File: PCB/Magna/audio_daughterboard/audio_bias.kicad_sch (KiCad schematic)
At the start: 8 parts, among them U1101 NE5532

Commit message: Some updates to PCB
Honestly I cannot remember whats changed
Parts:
- renumbered C1101 to C801, C1102 to C802, R1101 to R801, R1102 to R802, TP1101 to TP801, TP1102 to TP802, TP1103 to TP803, U1101 to U801

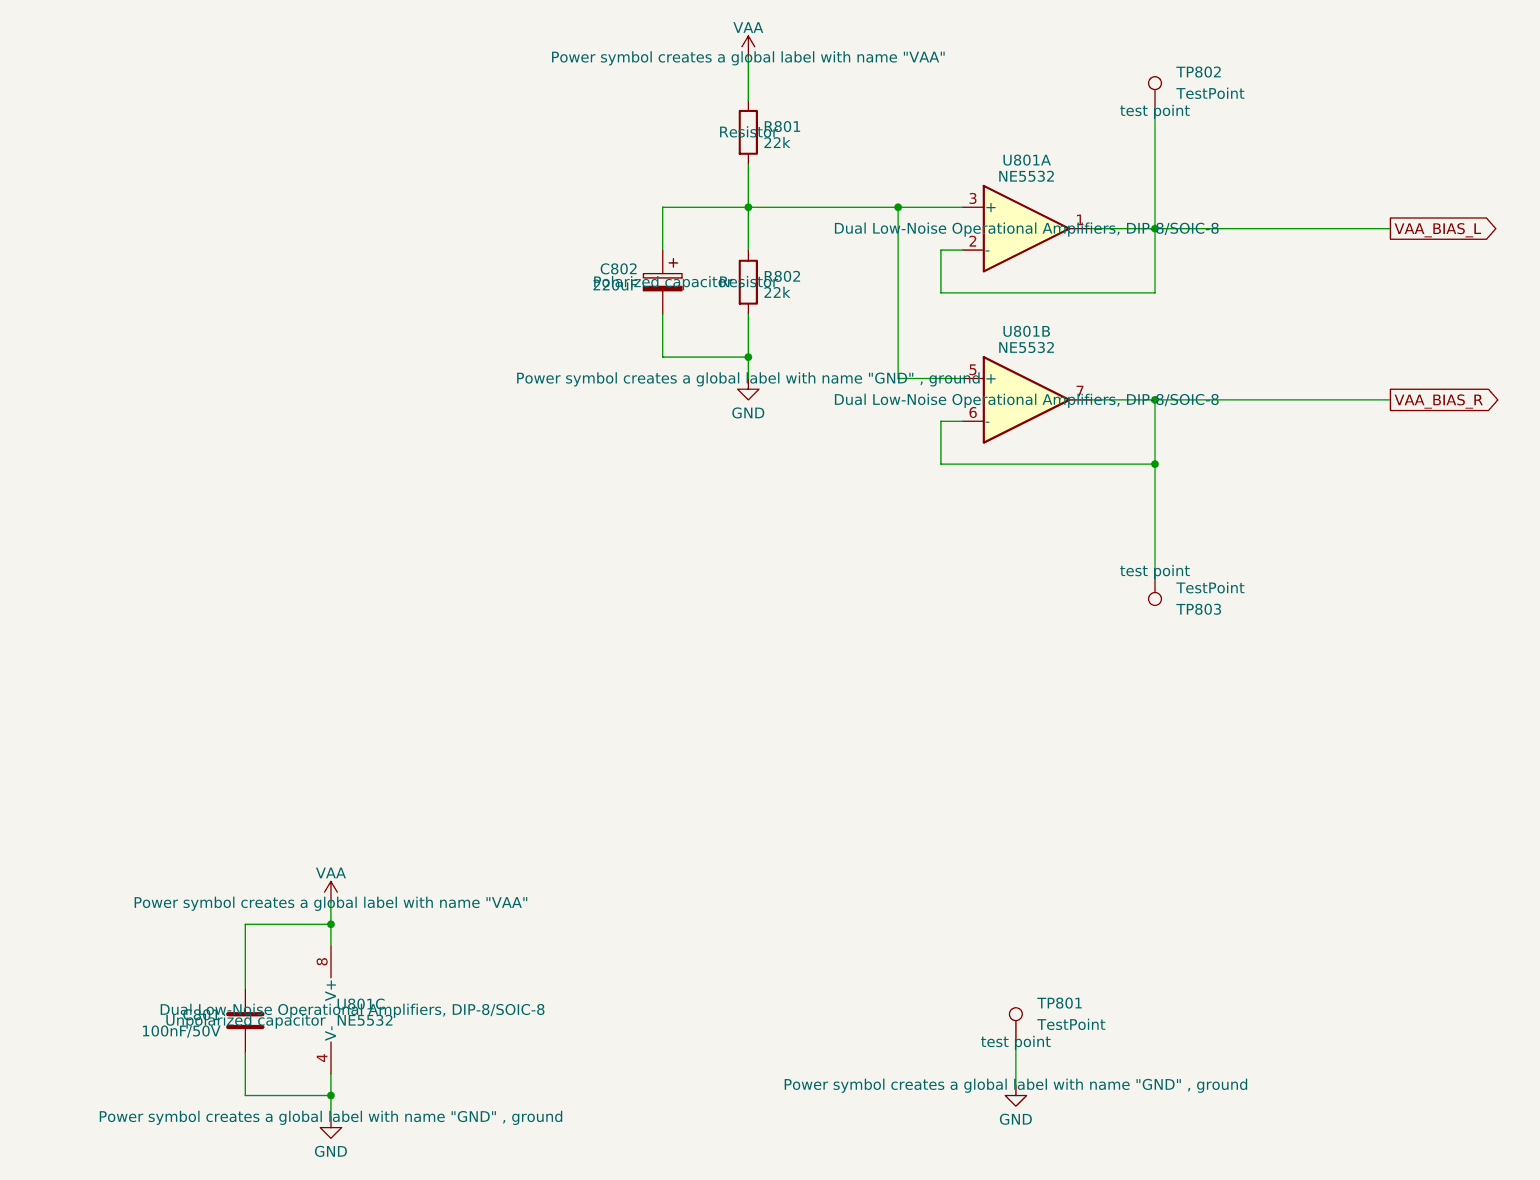
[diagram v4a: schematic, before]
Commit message: Update schematics to Kicad 9
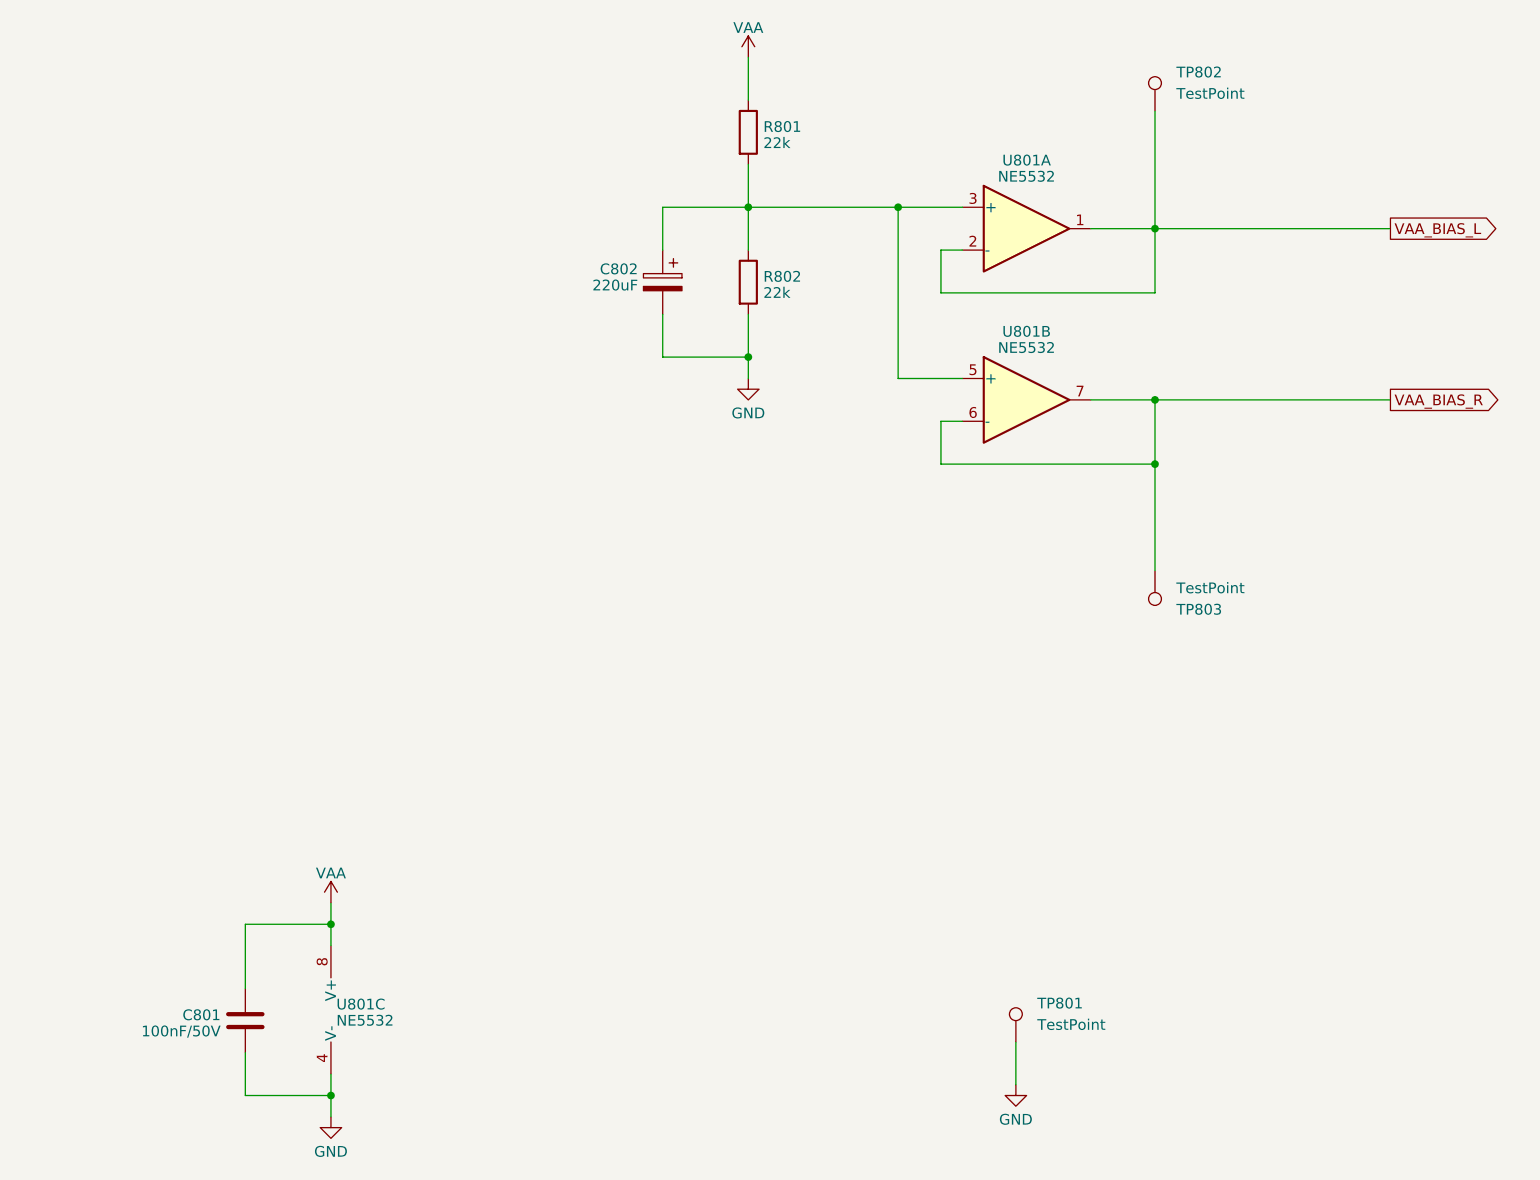
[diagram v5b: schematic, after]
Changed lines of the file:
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@@
 					(size 1.27 1.27)
 				)
+				(hide yes)
 			)
 		)
@@
 					(size 1.27 1.27)
 				)
+				(hide yes)
 			)
 		)
@@
 					(size 1.27 1.27)
 				)
+				(hide yes)
 			)
 		)
@@
 					(size 1.27 1.27)
 				)
+				(hide yes)
 			)
 		)
@@
 					(size 1.27 1.27)
 				)
+				(hide yes)
 			)
 		)
@@
 					(size 1.27 1.27)
 				)
+				(hide yes)
 			)
 		)
@@
 					(size 1.27 1.27)
 				)
+				(hide yes)
 			)
 		)
@@
 					(size 1.27 1.27)
 				)
+				(hide yes)
 			)
 		)
@@
 					(size 1.27 1.27)
 				)
+				(hide yes)
 			)
 		)
@@
 					(size 1.27 1.27)
 				)
+				(hide yes)
 			)
 		)
@@
 					(size 1.27 1.27)
 				)
+				(hide yes)
 			)
 		)
@@
 					(size 1.27 1.27)
 				)
+				(hide yes)
 			)
 		)
@@
 					(size 1.27 1.27)
 				)
+				(hide yes)
 			)
 		)
@@
 					(size 1.27 1.27)
 				)
+				(hide yes)
 			)
 		)
@@
 					(size 1.27 1.27)
 				)
-			)
-		)
+				(hide yes)
+			)
+		)

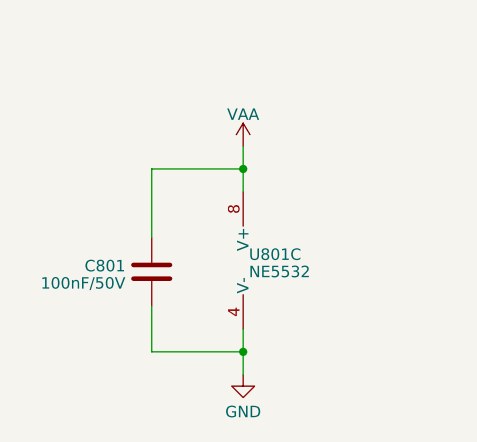
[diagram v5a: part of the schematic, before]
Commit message: Update audio PCB
Mainly added simulations to Linedriver and DAC.

Also fixed some small issues that was found when simulating
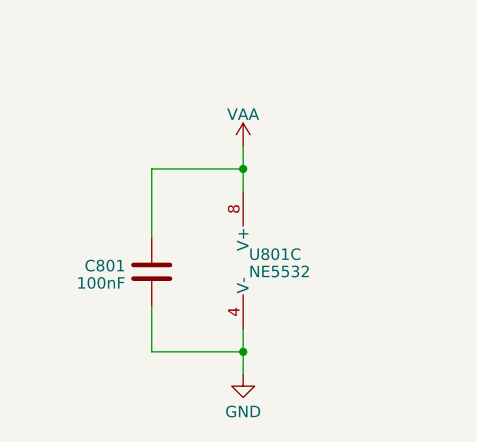
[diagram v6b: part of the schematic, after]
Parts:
- C801: value 100nF/50V -> 100nF
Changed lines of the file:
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@@
 			)
 		)
-		(property "Value" "100nF/50V"
+		(property "Value" "100nF"
 			(at 47.879 172.7273 0)
 			(effects
